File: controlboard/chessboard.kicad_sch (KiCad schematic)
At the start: 19 parts, among them J3 Conn_02x04_Counter_Clockwise, U3 AMS1117-3.3

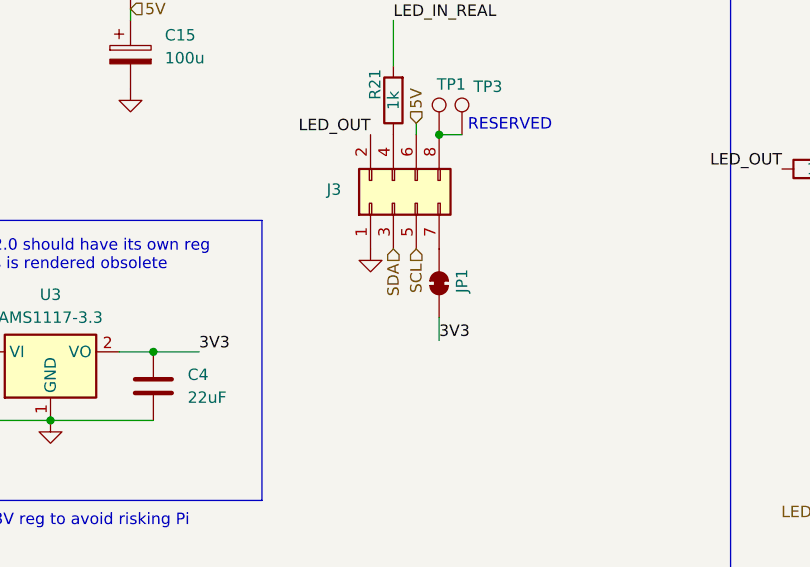
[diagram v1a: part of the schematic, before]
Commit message: Control board changes
Made a few control board changes (green checks on discord)
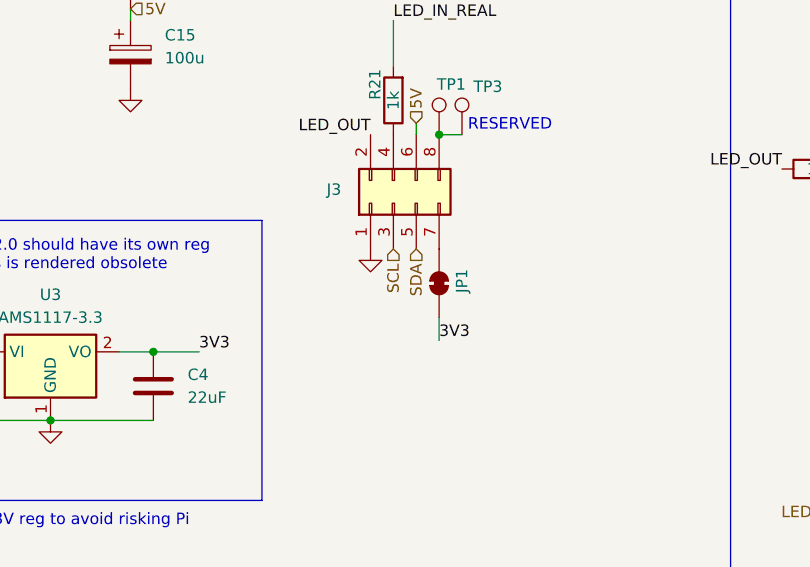
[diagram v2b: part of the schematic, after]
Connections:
- net SCL: now also J3.3 (Pin_3); no longer J3.5 (Pin_5)
- net SDA: now also J3.5 (Pin_5); no longer J3.3 (Pin_3)
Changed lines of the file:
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@@
-		)
-	)
-	(hierarchical_label "SCL"
-		(shape input)
-		(at 171.45 83.82 270)
-		(fields_autoplaced yes)
-		(effects
-			(font
-				(size 1.27 1.27)
-			)
-			(justify right)
 		)
 	)
@@
 		)
 	)
-	(hierarchical_label "SDA"
+	(hierarchical_label "SCL"
 		(shape input)
 		(at 168.91 83.82 270)
@@
 		)
 	)
+	(hierarchical_label "SDA"
+		(shape input)
+		(at 171.45 83.82 270)
+		(fields_autoplaced yes)
+		(effects
+			(font
+				(size 1.27 1.27)
+			)
+			(justify right)
+		)
+	)
